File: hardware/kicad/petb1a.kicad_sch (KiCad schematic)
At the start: 17 parts, among them J2 USB_C_Receptacle_USB2.0, U1 ESP32-S3-WROOM-1, U2 BME680, U3 XC6220B331MR, U4 USBLC6-2P6

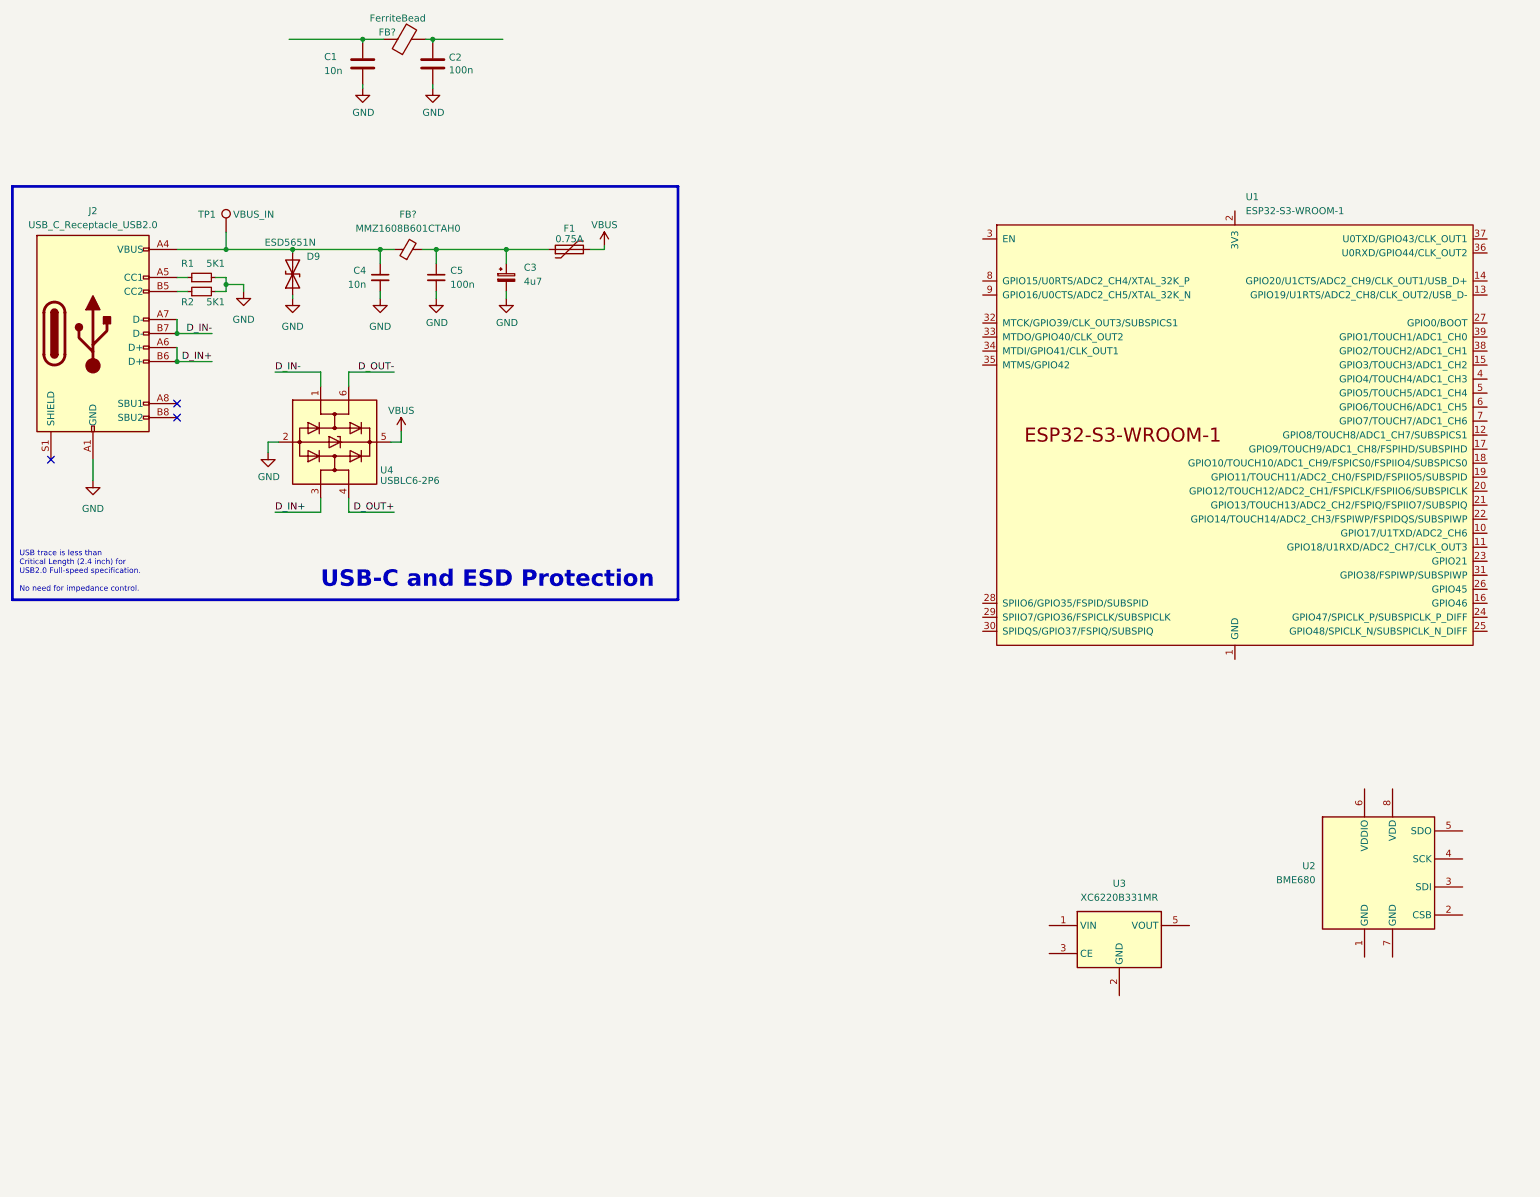
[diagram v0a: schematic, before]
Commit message: add reset, boot, ldo and bypass cap
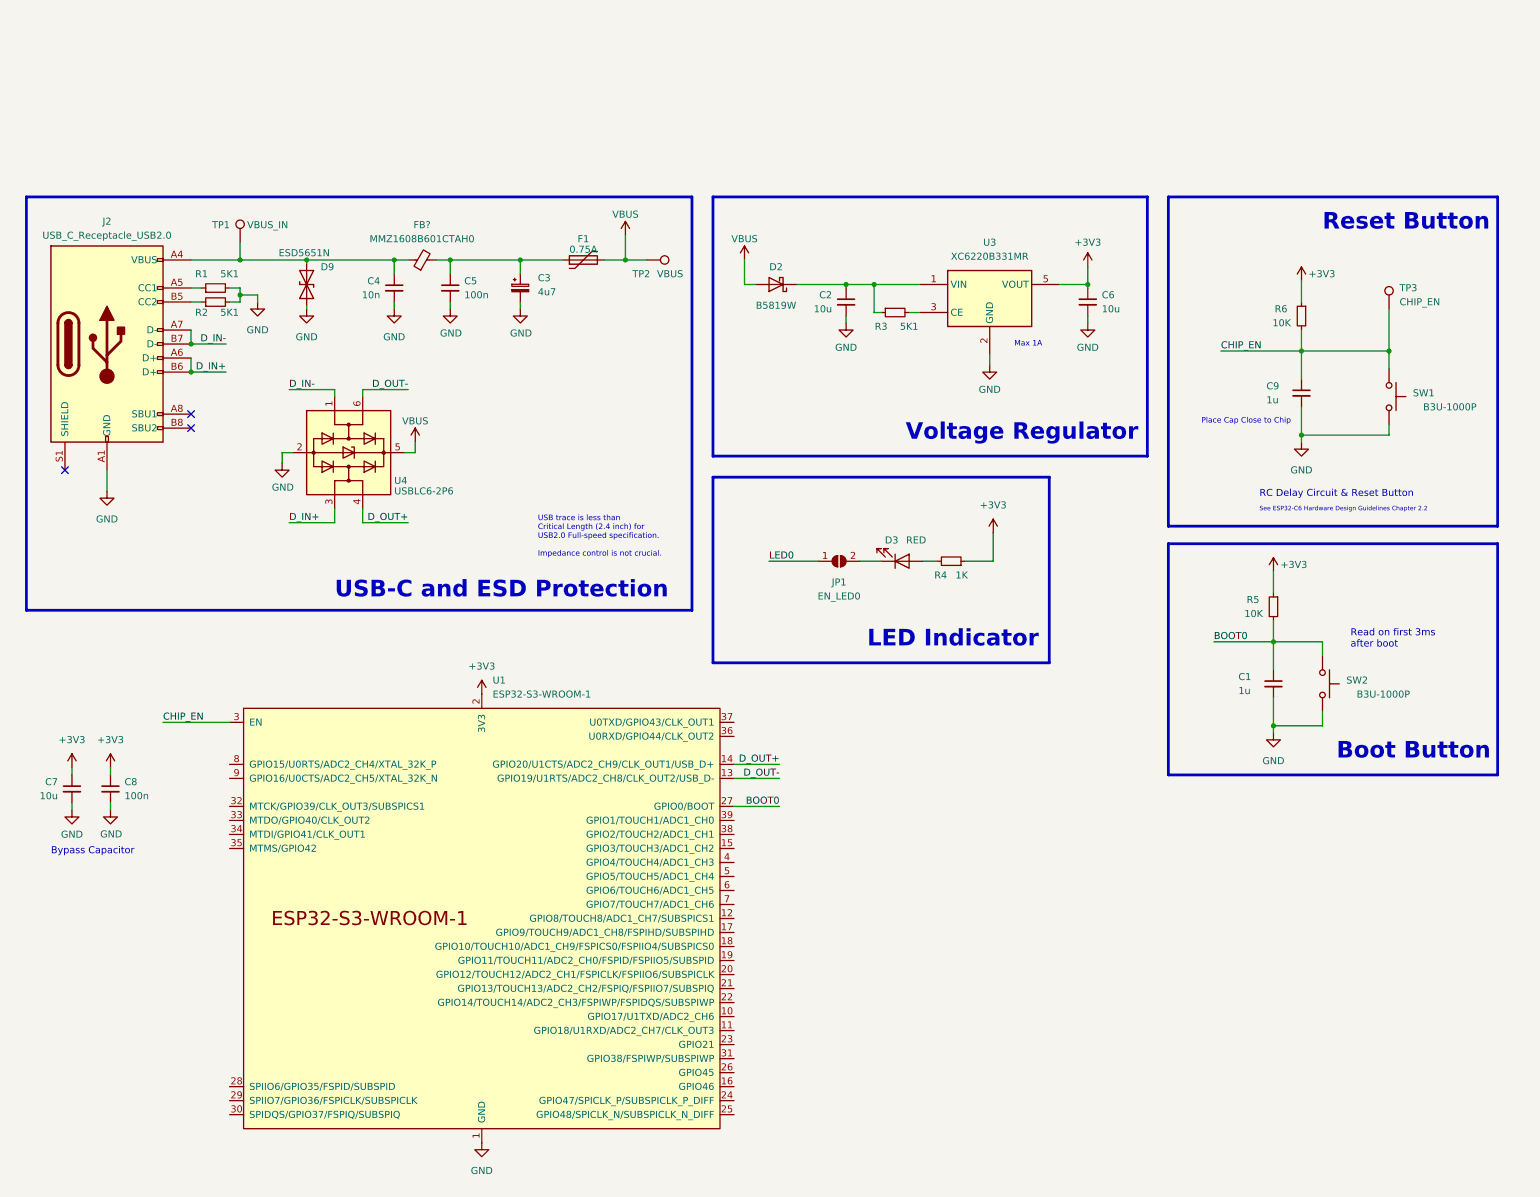
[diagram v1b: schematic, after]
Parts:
- removed C1: 10n, Capacitor_SMD:C_0402_1005Metric, symbol Device:C
- removed C2: 100n, Capacitor_SMD:C_0402_1005Metric, symbol Device:C
- removed FB?: FerriteBead, Inductor_SMD:L_0603_1608Metric, symbol Device:FerriteBead
- removed U2: BME680, Package_LGA:Bosch_LGA-8_3x3mm_P0.8mm_ClockwisePinNumbering, symbol Sensor:BME680
- added C1, C9: 1u, Capacitor_SMD:C_0402_1005Metric, symbol Device:C_Small
- added C2, C6, C7: 10u, symbol Device:C_Small
- added C8: 100n, symbol Device:C_Small
- added D2: B5819W, Diode_SMD:D_SOD-123, symbol Diode:MBR0540
- added D3: RED, LED_SMD:LED_0603_1608Metric, symbol Device:LED
- added JP1: EN_LED0, symbol Jumper:SolderJumper_2_Open
- added R3: 5K1, Resistor_SMD:R_0402_1005Metric, symbol Device:R_Small
- added R4: 1K, Resistor_SMD:R_0603_1608Metric, symbol Device:R_Small
- added R5, R6: 10K, Resistor_SMD:R_0402_1005Metric, symbol Device:R_Small
- added SW1, SW2: B3U-1000P, Button_Switch_SMD:SW_SPST_B3U-1000P, symbol Switch:SW_Push
- added TP2: VBUS, TestPoint:TestPoint_Pad_D1.0mm, symbol Connector:TestPoint
- added TP3: CHIP_EN, TestPoint:TestPoint_Pad_D1.0mm, symbol Connector:TestPoint
- C4: Part Description (none) -> Ceramic Capacitors 16V 10nF X7R ±10%
- C5: Part Description (none) -> Ceramic Capacitor 16V 100nF X7R ±10%
- FB?: footprint (none) -> Inductor_SMD:L_0603_1608Metric; Manufacturer (none) -> TDK; Manufacturer Part Number (none) -> MMZ1608B601CTAH0; Part Description (none) -> Ferrite Beads 400mΩ ±25% 600Ω@100MHz
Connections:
- net D_OUT+: now also U1.14 (GPIO20/U1CTS/ADC2_CH9/CLK_OUT1/USB_D+)
- net D_OUT-: now also U1.13 (GPIO19/U1RTS/ADC2_CH8/CLK_OUT2/USB_D-)
- net GND: now also U1.1 (GND), U1.40 (GND), U1.41 (GND), U3.2 (GND), C1.2, C2.2, C6.2, C7.2, C8.2, C9.2, SW1.1, SW2.1
- net VBUS: now also D2.2 (A), TP2.1
- net +3V3: now reaches U1.2 (3V3)
- net +3V3: now also U3.5 (VOUT), C6.1, C7.1, C8.1, R4.1, R5.1, R6.1
- net BOOT0: now reaches U1.27 (GPIO0/BOOT)
- net BOOT0: now also C1.1, R5.2, SW2.2
- net CHIP_EN: now reaches U1.3 (EN)
- net CHIP_EN: now also C9.1, R6.2, SW1.2, TP3.1
- net at U3.1 (VIN): now also C2.1, D2.1 (K), R3.1
- net at U3.3 (CE): now also R3.2
- new net: D3.2 (A), R4.2
- new net: D3.1 (K), JP1.2 (B)
- new net LED0: JP1.1 (A)
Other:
- note added: "Boot Button"
- note added: "Bypass Capacitor"
- note added: "LED Indicator"
- note added: "Max 1A"
- note added: "Place Cap Close to Chip"
- note added: "RC Delay Circuit & Reset Button"
- note added: "Read on first 3ms after boot"
- note added: "Reset Button"
- note added: "See ESP32-C6 Hardware Design Guidelines Chapter 2.2"
- note added: "USB trace is less than Critical Length (2.4 inch) for USB2.0 Full-speed specification. Impedance control is not crucial."
- note added: "Voltage Regulator"
- note removed: "USB trace is less than Critical Length (2.4 inch) for USB2.0 Full-speed specification. No need for impedance control."
- company: (none) -> Teapot Laboratories
- title: (none) -> PETB1A
- moved on the sheet: C3, C4, C5, D9, F1, FB?, J2, R1, R2, TP1, U1, U3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

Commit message: update schematic
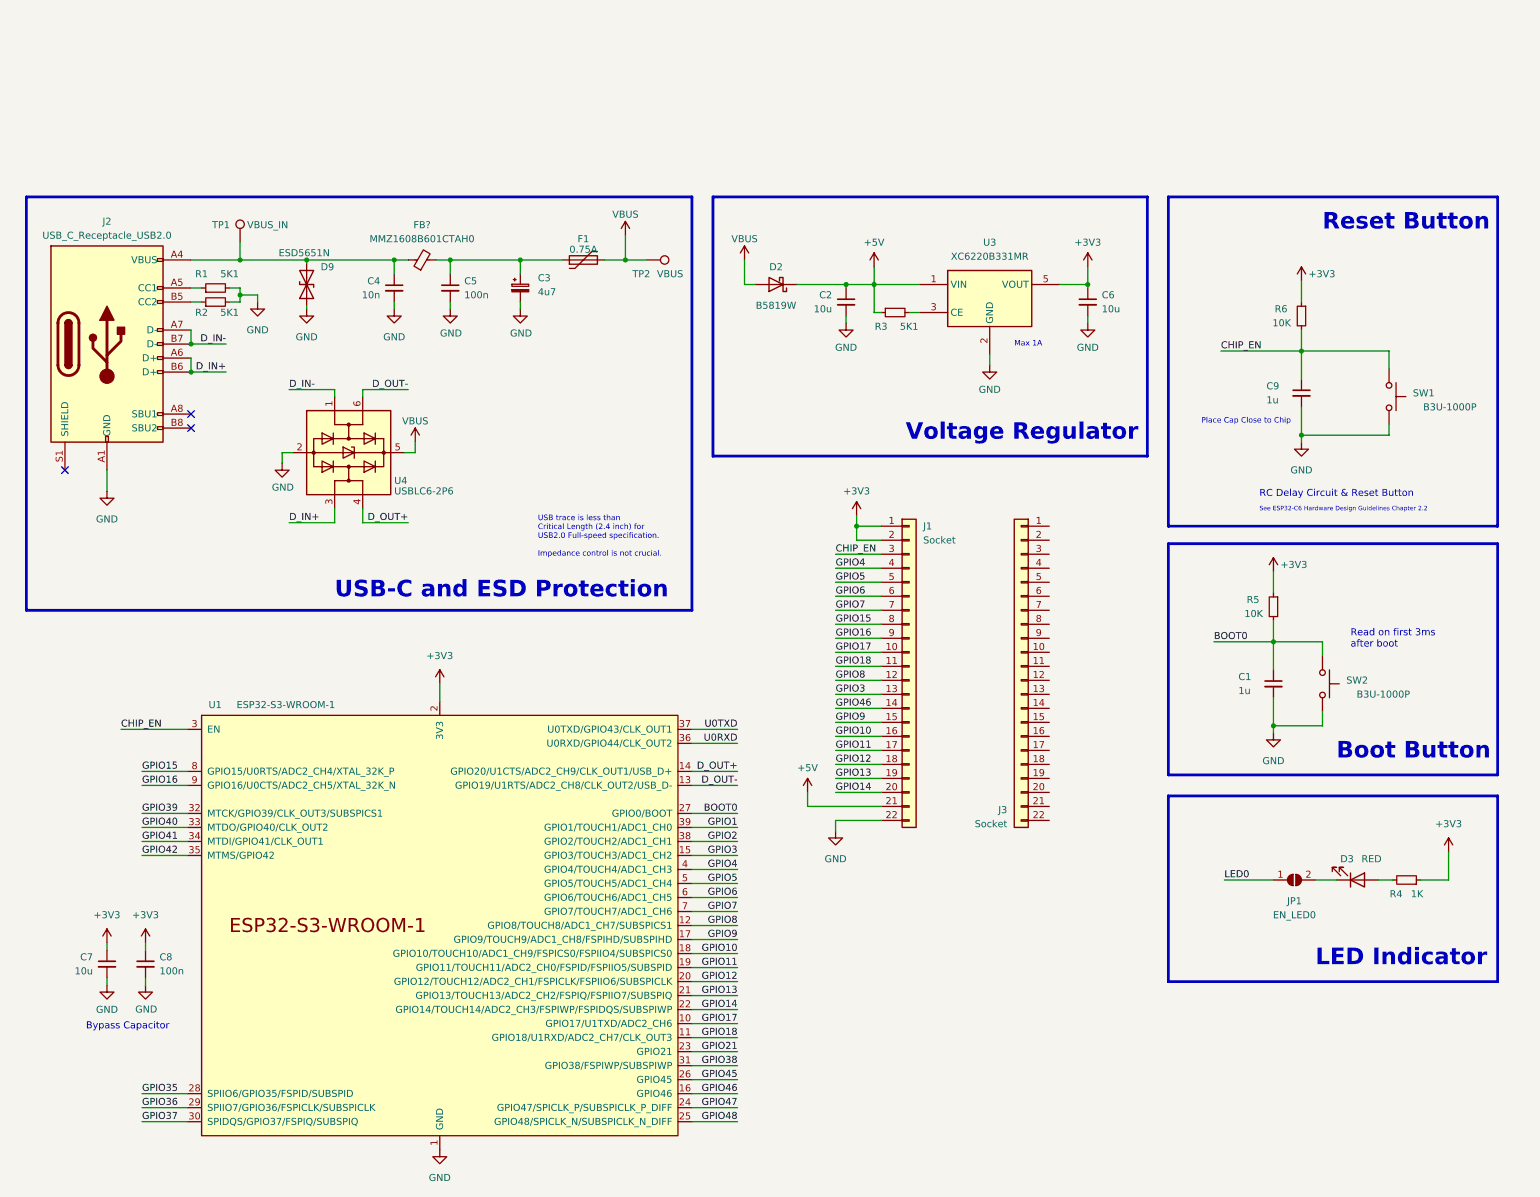
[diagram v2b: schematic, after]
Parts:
- removed TP3: CHIP_EN, TestPoint:TestPoint_Pad_D1.0mm, symbol Connector:TestPoint
- added J1, J3: Socket, symbol Connector_Generic:Conn_01x22
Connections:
- net +3V3: now also J1.1 (Pin_1), J1.2 (Pin_2)
- net CHIP_EN: now also J1.3 (Pin_3)
- net GND: now also J1.22 (Pin_22)
- net +5V: now reaches C2.1, D2.1 (K), R3.1, U3.1 (VIN)
- net +5V: now also J1.21 (Pin_21)
- net GPIO17: now reaches U1.10 (GPIO17/U1TXD/ADC2_CH6)
- net GPIO17: now also J1.10 (Pin_10)
- net GPIO18: now reaches U1.11 (GPIO18/U1RXD/ADC2_CH7/CLK_OUT3)
- net GPIO18: now also J1.11 (Pin_11)
- net GPIO8: now reaches U1.12 (GPIO8/TOUCH8/ADC1_CH7/SUBSPICS1)
- net GPIO8: now also J1.12 (Pin_12)
- net GPIO3: now reaches U1.15 (GPIO3/TOUCH3/ADC1_CH2)
- net GPIO3: now also J1.13 (Pin_13)
- net GPIO46: now reaches U1.16 (GPIO46)
- net GPIO46: now also J1.14 (Pin_14)
- net GPIO9: now reaches U1.17 (GPIO9/TOUCH9/ADC1_CH8/FSPIHD/SUBSPIHD)
- net GPIO9: now also J1.15 (Pin_15)
- net GPIO10: now reaches U1.18 (GPIO10/TOUCH10/ADC1_CH9/FSPICS0/FSPIIO4/SUBSPICS0)
- net GPIO10: now also J1.16 (Pin_16)
- net GPIO11: now reaches U1.19 (GPIO11/TOUCH11/ADC2_CH0/FSPID/FSPIIO5/SUBSPID)
- net GPIO11: now also J1.17 (Pin_17)
- net GPIO12: now reaches U1.20 (GPIO12/TOUCH12/ADC2_CH1/FSPICLK/FSPIIO6/SUBSPICLK)
- net GPIO12: now also J1.18 (Pin_18)
- net GPIO13: now reaches U1.21 (GPIO13/TOUCH13/ADC2_CH2/FSPIQ/FSPIIO7/SUBSPIQ)
- net GPIO13: now also J1.19 (Pin_19)
- net GPIO14: now reaches U1.22 (GPIO14/TOUCH14/ADC2_CH3/FSPIWP/FSPIDQS/SUBSPIWP)
- net GPIO14: now also J1.20 (Pin_20)
- net GPIO21: now reaches U1.23 (GPIO21)
- net GPIO47: now reaches U1.24 (GPIO47/SPICLK_P/SUBSPICLK_P_DIFF)
- net GPIO48: now reaches U1.25 (GPIO48/SPICLK_N/SUBSPICLK_N_DIFF)
- net GPIO45: now reaches U1.26 (GPIO45)
- net GPIO35: now reaches U1.28 (SPIIO6/GPIO35/FSPID/SUBSPID)
- net GPIO36: now reaches U1.29 (SPIIO7/GPIO36/FSPICLK/SUBSPICLK)
- net GPIO37: now reaches U1.30 (SPIDQS/GPIO37/FSPIQ/SUBSPIQ)
- net GPIO38: now reaches U1.31 (GPIO38/FSPIWP/SUBSPIWP)
- net GPIO39: now reaches U1.32 (MTCK/GPIO39/CLK_OUT3/SUBSPICS1)
- net GPIO40: now reaches U1.33 (MTDO/GPIO40/CLK_OUT2)
- net GPIO41: now reaches U1.34 (MTDI/GPIO41/CLK_OUT1)
- net GPIO42: now reaches U1.35 (MTMS/GPIO42)
- net U0RXD: now reaches U1.36 (U0RXD/GPIO44/CLK_OUT2)
- net U0TXD: now reaches U1.37 (U0TXD/GPIO43/CLK_OUT1)
- net GPIO2: now reaches U1.38 (GPIO2/TOUCH2/ADC1_CH1)
- net GPIO1: now reaches U1.39 (GPIO1/TOUCH1/ADC1_CH0)
- net GPIO4: now reaches U1.4 (GPIO4/TOUCH4/ADC1_CH3)
- net GPIO4: now also J1.4 (Pin_4)
- net GPIO5: now reaches U1.5 (GPIO5/TOUCH5/ADC1_CH4)
- net GPIO5: now also J1.5 (Pin_5)
- net GPIO6: now reaches U1.6 (GPIO6/TOUCH6/ADC1_CH5)
- net GPIO6: now also J1.6 (Pin_6)
- net GPIO7: now reaches U1.7 (GPIO7/TOUCH7/ADC1_CH6)
- net GPIO7: now also J1.7 (Pin_7)
- net GPIO15: now reaches U1.8 (GPIO15/U0RTS/ADC2_CH4/XTAL_32K_P)
- net GPIO15: now also J1.8 (Pin_8)
- net GPIO16: now reaches U1.9 (GPIO16/U0CTS/ADC2_CH5/XTAL_32K_N)
- net GPIO16: now also J1.9 (Pin_9)
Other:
- moved on the sheet: C7, C8, D3, JP1, R4, U1
